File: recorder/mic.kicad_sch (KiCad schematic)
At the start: 3 parts, among them U1 IM73D122V01

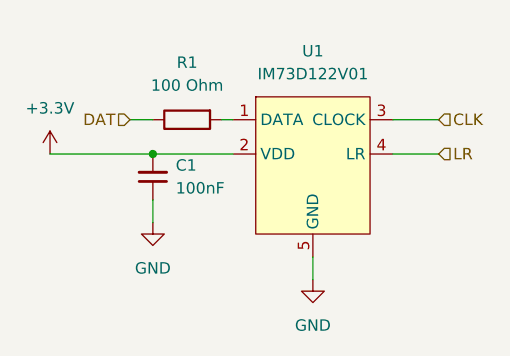
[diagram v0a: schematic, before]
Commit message: added LDO
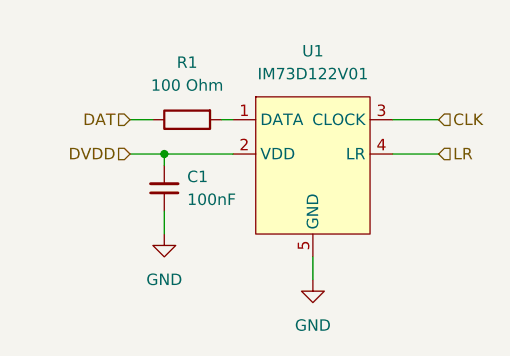
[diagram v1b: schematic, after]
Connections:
- net +3.3V renamed DVDD
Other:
- moved on the sheet: C1
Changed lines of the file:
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@@
 	(paper "A4")
 	(junction
-		(at 121.92 83.82)
+		(at 123.19 83.82)
 		(diameter 0)
 		(color 0 0 0 0)
@@
 	(wire
 		(pts
+			(xy 123.19 90.17) (xy 123.19 92.71)
+		)
+		(stroke
+			(width 0)
+			(type default)
+		)
+	)
+	(wire
+		(pts
 			(xy 148.59 83.82) (xy 153.67 83.82)
 		)
@@
 	(wire
 		(pts
-			(xy 121.92 83.82) (xy 130.81 83.82)
+			(xy 123.19 83.82) (xy 130.81 83.82)
 		)
 		(stroke
@@
 	(wire
 		(pts
-			(xy 121.92 88.9) (xy 121.92 91.44)
+			(xy 123.19 85.09) (xy 123.19 83.82)
 		)
 		(stroke
@@
 	(wire
 		(pts
-			(xy 110.49 83.82) (xy 121.92 83.82)
+			(xy 119.38 83.82) (xy 123.19 83.82)
 		)
 		(stroke
@@
 			)
 			(justify left)
+		)
+	)
+	(hierarchical_label "DVDD"
+		(shape input)
+		(at 119.38 83.82 180)
+		(effects
+			(font
+				(size 1.27 1.27)
+			)
+			(justify right)
 		)
 	)
@@
 		(instances
 			(project "recorder"
-				(path "/f8461171-9f32-4945-9984-5de8e21a02d2/c2ec8492-3a88-4bf8-959e-131abfaefa09"
+				(path "/f8461171-9f32-4945-9984-5de8e21a02d2/18adc8f8-84a3-4040-80c8-8dec34235bde"
+					(reference "U6")
+					(unit 1)
+				)
+				(path "/f8461171-9f32-4945-9984-5de8e21a02d2/26e270d8-30bf-4e33-a83d-78a767ff8d6d"
+					(reference "U8")
+					(unit 1)
+				)
+				(path "/f8461171-9f32-4945-9984-5de8e21a02d2/4caf5b05-5142-46d8-9838-1305320703c5"
+					(reference "U9")
+					(unit 1)
+				)
+				(path "/f8461171-9f32-4945-9984-5de8e21a02d2/51cb2aa5-e01a-4a1f-ab57-d2276ebfacb2"
+					(reference "U5")
+					(unit 1)
+				)
+				(path "/f8461171-9f32-4945-9984-5de8e21a02d2/546ac693-77f8-4549-8910-cfded033dd3d"
+					(reference "U4")
+					(unit 1)
+				)
+				(path "/f8461171-9f32-4945-9984-5de8e21a02d2/a1c54d07-c0b6-4712-97aa-a1d686bd1270"
+					(reference "U7")
+					(unit 1)
+				)
+				(path "/f8461171-9f32-4945-9984-5de8e21a02d2/b19ed33f-832d-49a5-9063-a6934bf07b17"
 					(reference "U3")
 					(unit 1)
@@
 		(instances
 			(project "recorder"
-				(path "/f8461171-9f32-4945-9984-5de8e21a02d2/c2ec8492-3a88-4bf8-959e-131abfaefa09"
+				(path "/f8461171-9f32-4945-9984-5de8e21a02d2/18adc8f8-84a3-4040-80c8-8dec34235bde"
+					(reference "R5")
+					(unit 1)
+				)
+				(path "/f8461171-9f32-4945-9984-5de8e21a02d2/26e270d8-30bf-4e33-a83d-78a767ff8d6d"
+					(reference "R7")
+					(unit 1)
+				)
+				(path "/f8461171-9f32-4945-9984-5de8e21a02d2/4caf5b05-5142-46d8-9838-1305320703c5"
+					(reference "R8")
+					(unit 1)
+				)
+				(path "/f8461171-9f32-4945-9984-5de8e21a02d2/51cb2aa5-e01a-4a1f-ab57-d2276ebfacb2"
+					(reference "R4")
+					(unit 1)
+				)
+				(path "/f8461171-9f32-4945-9984-5de8e21a02d2/546ac693-77f8-4549-8910-cfded033dd3d"
+					(reference "R3")
+					(unit 1)
+				)
+				(path "/f8461171-9f32-4945-9984-5de8e21a02d2/a1c54d07-c0b6-4712-97aa-a1d686bd1270"
+					(reference "R6")
+					(unit 1)
+				)
+				(path "/f8461171-9f32-4945-9984-5de8e21a02d2/b19ed33f-832d-49a5-9063-a6934bf07b17"
 					(reference "R2")
 					(unit 1)
@@
 	(symbol
 		(lib_id "power:GND")
-		(at 121.92 91.44 0)
+		(at 123.19 92.71 0)
 		(unit 1)
 		(exclude_from_sim no)
@@
 		(fields_autoplaced yes)
 		(property "Reference" "#PWR06"
-			(at 121.92 97.79 0)
+			(at 123.19 99.06 0)
 			(effects
 				(font
@@
 		)
 		(property "Value" "GND"
-			(at 121.92 96.52 0)
+			(at 123.19 97.79 0)
 			(effects
 				(font
@@
 		)
 		(property "Footprint" ""
-			(at 121.92 91.44 0)
+			(at 123.19 92.71 0)
 			(effects
 				(font
@@
 		)
 		(property "Datasheet" ""
-			(at 121.92 91.44 0)
+			(at 123.19 92.71 0)
 			(effects
 				(font
@@
 		)
 		(property "Description" "Power symbol creates a global label with name \"GND\" , ground"
-			(at 121.92 91.44 0)
+			(at 123.19 92.71 0)
 			(effects
 				(font
@@
 		(instances
 			(project "recorder"
-				(path "/f8461171-9f32-4945-9984-5de8e21a02d2/c2ec8492-3a88-4bf8-959e-131abfaefa09"
+				(path "/f8461171-9f32-4945-9984-5de8e21a02d2/18adc8f8-84a3-4040-80c8-8dec34235bde"
+					(reference "#PWR013")
+					(unit 1)
+				)
+				(path "/f8461171-9f32-4945-9984-5de8e21a02d2/26e270d8-30bf-4e33-a83d-78a767ff8d6d"
+					(reference "#PWR023")
+					(unit 1)
+				)
+				(path "/f8461171-9f32-4945-9984-5de8e21a02d2/4caf5b05-5142-46d8-9838-1305320703c5"
+					(reference "#PWR025")
+					(unit 1)
+				)
+				(path "/f8461171-9f32-4945-9984-5de8e21a02d2/51cb2aa5-e01a-4a1f-ab57-d2276ebfacb2"
+					(reference "#PWR011")
+					(unit 1)
+				)
+				(path "/f8461171-9f32-4945-9984-5de8e21a02d2/546ac693-77f8-4549-8910-cfded033dd3d"
+					(reference "#PWR09")
+					(unit 1)
+				)
+				(path "/f8461171-9f32-4945-9984-5de8e21a02d2/a1c54d07-c0b6-4712-97aa-a1d686bd1270"
+					(reference "#PWR015")
+					(unit 1)
+				)
+				(path "/f8461171-9f32-4945-9984-5de8e21a02d2/b19ed33f-832d-49a5-9063-a6934bf07b17"
 					(reference "#PWR07")
 					(unit 1)
@@
 	(symbol
 		(lib_id "recorder:C_Small_1")
-		(at 121.92 86.36 180)
+		(at 123.19 87.63 180)
 		(unit 1)
 		(exclude_from_sim no)
@@
 		(fields_autoplaced yes)
 		(property "Reference" "C1"
-			(at 124.46 85.0835 0)
+			(at 125.73 86.3535 0)
 			(effects
 				(font
@@
 		)
 		(property "Value" "100nF"
-			(at 124.46 87.6235 0)
+			(at 125.73 88.8935 0)
 			(effects
 				(font
@@
 		)
 		(property "Footprint" ""
-			(at 121.92 86.36 0)
+			(at 123.19 87.63 0)
 			(effects
 				(font
@@
 		)
 		(property "Datasheet" "~"
-			(at 121.92 86.36 0)
+			(at 123.19 87.63 0)
 			(effects
 				(font
@@
 		)
 		(property "Description" "Unpolarized capacitor, small symbol"
-			(at 121.92 86.36 0)
+			(at 123.19 87.63 0)
 			(effects
 				(font
@@
 		(instances
 			(project "recorder"
-				(path "/f8461171-9f32-4945-9984-5de8e21a02d2/c2ec8492-3a88-4bf8-959e-131abfaefa09"
+				(path "/f8461171-9f32-4945-9984-5de8e21a02d2/18adc8f8-84a3-4040-80c8-8dec34235bde"
+					(reference "C5")
+					(unit 1)
+				)
+				(path "/f8461171-9f32-4945-9984-5de8e21a02d2/26e270d8-30bf-4e33-a83d-78a767ff8d6d"
+					(reference "C7")
+					(unit 1)
+				)
+				(path "/f8461171-9f32-4945-9984-5de8e21a02d2/4caf5b05-5142-46d8-9838-1305320703c5"
+					(reference "C8")
+					(unit 1)
+				)
+				(path "/f8461171-9f32-4945-9984-5de8e21a02d2/51cb2aa5-e01a-4a1f-ab57-d2276ebfacb2"
+					(reference "C4")
+					(unit 1)
+				)
+				(path "/f8461171-9f32-4945-9984-5de8e21a02d2/546ac693-77f8-4549-8910-cfded033dd3d"
+					(reference "C3")
+					(unit 1)
+				)
+				(path "/f8461171-9f32-4945-9984-5de8e21a02d2/a1c54d07-c0b6-4712-97aa-a1d686bd1270"
+					(reference "C6")
+					(unit 1)
+				)
+				(path "/f8461171-9f32-4945-9984-5de8e21a02d2/b19ed33f-832d-49a5-9063-a6934bf07b17"
 					(reference "C2")
 					(unit 1)
@@
 		(instances
 			(project "recorder"
-				(path "/f8461171-9f32-4945-9984-5de8e21a02d2/c2ec8492-3a88-4bf8-959e-131abfaefa09"
+				(path "/f8461171-9f32-4945-9984-5de8e21a02d2/18adc8f8-84a3-4040-80c8-8dec34235bde"
+					(reference "#PWR014")
+					(unit 1)
+				)
+				(path "/f8461171-9f32-4945-9984-5de8e21a02d2/26e270d8-30bf-4e33-a83d-78a767ff8d6d"
+					(reference "#PWR024")
+					(unit 1)
+				)
+				(path "/f8461171-9f32-4945-9984-5de8e21a02d2/4caf5b05-5142-46d8-9838-1305320703c5"
+					(reference "#PWR027")
+					(unit 1)
+				)
+				(path "/f8461171-9f32-4945-9984-5de8e21a02d2/51cb2aa5-e01a-4a1f-ab57-d2276ebfacb2"
+					(reference "#PWR012")
+					(unit 1)
+				)
+				(path "/f8461171-9f32-4945-9984-5de8e21a02d2/546ac693-77f8-4549-8910-cfded033dd3d"
+					(reference "#PWR010")
+					(unit 1)
+				)
+				(path "/f8461171-9f32-4945-9984-5de8e21a02d2/a1c54d07-c0b6-4712-97aa-a1d686bd1270"
+					(reference "#PWR022")
+					(unit 1)
+				)
+				(path "/f8461171-9f32-4945-9984-5de8e21a02d2/b19ed33f-832d-49a5-9063-a6934bf07b17"
 					(reference "#PWR08")
 					(unit 1)
@@
 					(unit 1)
 				)
-			)
-		)
-	)
-	(symbol
-		(lib_id "power:+3.3V")
-		(at 110.49 83.82 0)
-		(unit 1)
-		(exclude_from_sim no)
-		(in_bom yes)
-		(on_board yes)
-		(dnp no)
-		(fields_autoplaced yes)
-		(property "Reference" "#PWR03"
-			(at 110.49 87.63 0)
-			(effects
-				(font
-					(size 1.27 1.27)
-				)
-				(hide yes)
-			)
-		)
-		(property "Value" "+3.3V"
-			(at 110.49 78.74 0)
-			(effects
-				(font
-					(size 1.27 1.27)
-				)
-			)
-		)
-		(property "Footprint" ""
-			(at 110.49 83.82 0)
-			(effects
-				(font
-					(size 1.27 1.27)
-				)
-				(hide yes)
-			)
-		)
-		(property "Datasheet" ""
-			(at 110.49 83.82 0)
-			(effects
-				(font
-					(size 1.27 1.27)
-				)
-				(hide yes)
-			)
-		)
-		(property "Description" "Power symbol creates a global label with name \"+3.3V\""
-			(at 110.49 83.82 0)
-			(effects
-				(font
-					(size 1.27 1.27)
-				)
-				(hide yes)
-			)
-		)
-		(pin "1"
-		)
-		(instances
-			(project "recorder"
-				(path "/f8461171-9f32-4945-9984-5de8e21a02d2/c2ec8492-3a88-4bf8-959e-131abfaefa09"
-					(reference "#PWR04")
-					(unit 1)
-				)
-				(path "/f8461171-9f32-4945-9984-5de8e21a02d2/c45fdb6e-e38a-49e7-9e81-4b95b9080f0a"
-					(reference "#PWR03")
-					(unit 1)
-				)

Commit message: spaced out microphones
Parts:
- C1: footprint (none) -> Library:C_0603_1608Metric
- R1: value 100 Ohm -> 100; footprint (none) -> Library:R_0603_1608Metric; symbol recorder:R100 -> recorder:R
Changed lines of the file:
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@@
 	)
 	(symbol
-		(lib_id "recorder:R100")
+		(lib_id "recorder:R")
 		(at 125.73 80.01 270)
 		(unit 1)
@@
 			)
 		)
-		(property "Value" "100 Ohm"
+		(property "Value" "100"
 			(at 125.73 76.2 90)
 			(effects
@@
 			)
 		)
-		(property "Footprint" ""
+		(property "Footprint" "Library:R_0603_1608Metric"
 			(at 125.73 78.232 90)
 			(effects
@@
 			)
 		)
-		(property "Footprint" ""
+		(property "Footprint" "Library:C_0603_1608Metric"
 			(at 123.19 87.63 0)
 			(effects

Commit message: MPN and Package
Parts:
- C1: MPN (none) -> MCASJ168BD7475KTCA01; Package (none) -> 0603 (1608 Metric)
- R1: Package (none) -> 0603 (1608 Metric)
- U1: MPN (none) -> IM73D122V01XTMA1; Manufacturer (none) -> Infineon Technologies; Package (none) -> LGA-5
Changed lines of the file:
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@@
+			)
+		)
+		(property "Manufacturer" "Infineon Technologies"
+			(at 139.7 85.09 0)
+			(effects
+				(font
+					(size 1.27 1.27)
+				)
+				(hide yes)
+			)
+		)
+		(property "MPN" "IM73D122V01XTMA1"
+			(at 139.7 85.09 0)
+			(effects
+				(font
+					(size 1.27 1.27)
+				)
+				(hide yes)
+			)
+		)
+		(property "Package" "LGA-5"
+			(at 139.7 85.09 0)
+			(effects
+				(font
+					(size 1.27 1.27)
+				)
+				(hide yes)
 			)
 		)
@@
 			)
 		)
+		(property "Package" "0603 (1608 Metric)"
+			(at 125.73 80.01 0)
+			(effects
+				(font
+					(size 1.27 1.27)
+				)
+			)
+		)
 		(pin "2"
 		)
@@
 			)
 		)
+		(property "MPN" "MCASJ168BD7475KTCA01"
+			(at 123.19 87.63 0)
+			(effects
+				(font
+					(size 1.27 1.27)
+				)
+			)
+		)
+		(property "Package" "0603 (1608 Metric)"
+			(at 123.19 87.63 0)
+			(effects
+				(font
+					(size 1.27 1.27)
+				)
+			)
+		)

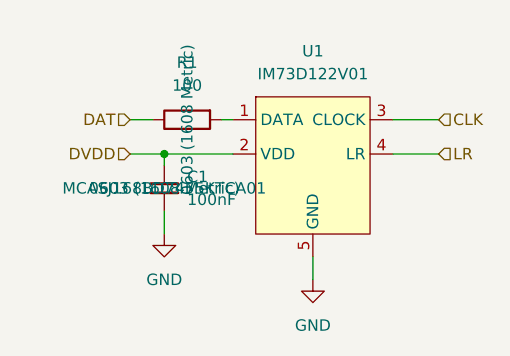
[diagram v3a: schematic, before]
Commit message: Polarization check of Capacitors
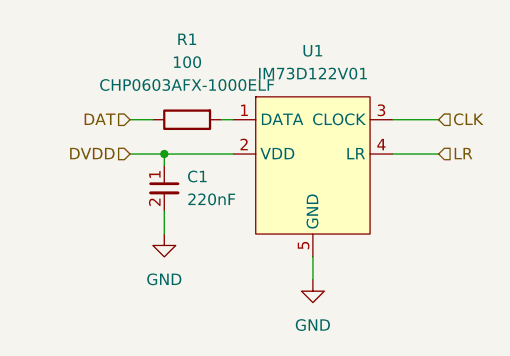
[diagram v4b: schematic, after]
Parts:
- C1: value 100nF -> 220nF; symbol recorder:C_Small_1 -> recorder:C_220nF; MPN MCASJ168BD7475KTCA01 -> 06036C223KAT2A
- R1: symbol recorder:R -> recorder:R_100; MPN (none) -> CHP0603AFX-1000ELF
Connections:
- net DVDD: now also C1.1; no longer C1.2
- net GND: now also C1.2; no longer C1.1
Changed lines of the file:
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@@
 	)
 	(symbol
-		(lib_id "recorder:R")
+		(lib_id "recorder:R_100")
 		(at 125.73 80.01 270)
 		(unit 1)
@@
 		(fields_autoplaced yes)
 		(property "Reference" "R1"
+			(at 125.73 71.12 90)
+			(effects
+				(font
+					(size 1.27 1.27)
+				)
+			)
+		)
+		(property "Value" "100"
 			(at 125.73 73.66 90)
-			(effects
-				(font
-					(size 1.27 1.27)
-				)
-			)
-		)
-		(property "Value" "100"
-			(at 125.73 76.2 90)
 			(effects
 				(font
@@
 		(property "Package" "0603 (1608 Metric)"
 			(at 125.73 80.01 0)
+			(effects
+				(font
+					(size 1.27 1.27)
+				)
+				(hide yes)
+			)
+		)
+		(property "MPN" "CHP0603AFX-1000ELF"
+			(at 125.73 76.2 90)
 			(effects
 				(font
@@
 		(dnp no)
 		(fields_autoplaced yes)
-		(property "Reference" "#PWR06"
+		(property "Reference" "#PWR6"
 			(at 123.19 99.06 0)
 			(effects
@@
 			(project "recorder"
 				(path "/f8461171-9f32-4945-9984-5de8e21a02d2/18adc8f8-84a3-4040-80c8-8dec34235bde"
-					(reference "#PWR013")
+					(reference "#PWR13")
 					(unit 1)
 				)
 				(path "/f8461171-9f32-4945-9984-5de8e21a02d2/26e270d8-30bf-4e33-a83d-78a767ff8d6d"
-					(reference "#PWR023")
+					(reference "#PWR23")
 					(unit 1)
 				)
 				(path "/f8461171-9f32-4945-9984-5de8e21a02d2/4caf5b05-5142-46d8-9838-1305320703c5"
-					(reference "#PWR025")
+					(reference "#PWR25")
 					(unit 1)
 				)
 				(path "/f8461171-9f32-4945-9984-5de8e21a02d2/51cb2aa5-e01a-4a1f-ab57-d2276ebfacb2"
-					(reference "#PWR011")
+					(reference "#PWR11")
 					(unit 1)
 				)
 				(path "/f8461171-9f32-4945-9984-5de8e21a02d2/546ac693-77f8-4549-8910-cfded033dd3d"
-					(reference "#PWR09")
+					(reference "#PWR9")
 					(unit 1)
 				)
 				(path "/f8461171-9f32-4945-9984-5de8e21a02d2/a1c54d07-c0b6-4712-97aa-a1d686bd1270"
-					(reference "#PWR015")
+					(reference "#PWR15")
 					(unit 1)
 				)
 				(path "/f8461171-9f32-4945-9984-5de8e21a02d2/b19ed33f-832d-49a5-9063-a6934bf07b17"
-					(reference "#PWR07")
+					(reference "#PWR7")
 					(unit 1)
 				)
 				(path "/f8461171-9f32-4945-9984-5de8e21a02d2/c45fdb6e-e38a-49e7-9e81-4b95b9080f0a"
-					(reference "#PWR06")
+					(reference "#PWR6")
 					(unit 1)
 				)
@@
 	)
 	(symbol
-		(lib_id "recorder:C_Small_1")
-		(at 123.19 87.63 180)
+		(lib_id "recorder:C_220nF")
+		(at 123.19 87.63 0)
 		(unit 1)
 		(exclude_from_sim no)
@@
 		(fields_autoplaced yes)
 		(property "Reference" "C1"
-			(at 125.73 86.3535 0)
-			(effects
-				(font
-					(size 1.27 1.27)
-				)
-				(justify right)
-			)
-		)
-		(property "Value" "100nF"
-			(at 125.73 88.8935 0)
-			(effects
-				(font
-					(size 1.27 1.27)
-				)
-				(justify right)
+			(at 125.73 86.3662 0)
+			(effects
+				(font
+					(size 1.27 1.27)
+				)
+				(justify left)
+			)
+		)
+		(property "Value" "220nF"
+			(at 125.73 88.9062 0)
+			(effects
+				(font
+					(size 1.27 1.27)
+				)
+				(justify left)
 			)
 		)
@@
 			)
 		)
-		(property "MPN" "MCASJ168BD7475KTCA01"
+		(property "MPN" " 06036C223KAT2A"
 			(at 123.19 87.63 0)
 			(effects
@@
 					(size 1.27 1.27)
 				)
+				(hide yes)
 			)
 		)
@@
 					(size 1.27 1.27)
 				)
+				(hide yes)
 			)
 		)
@@
 		(dnp no)
 		(fields_autoplaced yes)
-		(property "Reference" "#PWR05"
+		(property "Reference" "#PWR5"
 			(at 139.7 104.14 0)
 			(effects
@@
 			(project "recorder"
 				(path "/f8461171-9f32-4945-9984-5de8e21a02d2/18adc8f8-84a3-4040-80c8-8dec34235bde"
-					(reference "#PWR014")
+					(reference "#PWR14")
 					(unit 1)
 				)
 				(path "/f8461171-9f32-4945-9984-5de8e21a02d2/26e270d8-30bf-4e33-a83d-78a767ff8d6d"
-					(reference "#PWR024")
+					(reference "#PWR24")
 					(unit 1)
 				)
 				(path "/f8461171-9f32-4945-9984-5de8e21a02d2/4caf5b05-5142-46d8-9838-1305320703c5"
-					(reference "#PWR027")
+					(reference "#PWR27")
 					(unit 1)
 				)
 				(path "/f8461171-9f32-4945-9984-5de8e21a02d2/51cb2aa5-e01a-4a1f-ab57-d2276ebfacb2"
-					(reference "#PWR012")
+					(reference "#PWR12")
 					(unit 1)
 				)
 				(path "/f8461171-9f32-4945-9984-5de8e21a02d2/546ac693-77f8-4549-8910-cfded033dd3d"
-					(reference "#PWR010")
+					(reference "#PWR10")
 					(unit 1)
 				)
 				(path "/f8461171-9f32-4945-9984-5de8e21a02d2/a1c54d07-c0b6-4712-97aa-a1d686bd1270"
-					(reference "#PWR022")
+					(reference "#PWR22")
 					(unit 1)
 				)
 				(path "/f8461171-9f32-4945-9984-5de8e21a02d2/b19ed33f-832d-49a5-9063-a6934bf07b17"
-					(reference "#PWR08")
+					(reference "#PWR8")
 					(unit 1)
 				)
 				(path "/f8461171-9f32-4945-9984-5de8e21a02d2/c45fdb6e-e38a-49e7-9e81-4b95b9080f0a"
-					(reference "#PWR05")
-					(unit 1)
-				)
+					(reference "#PWR5")
+					(unit 1)
+				)
